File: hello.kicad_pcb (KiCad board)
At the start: 2 copper layers, 50 x 50 mm, 56 parts, among them J1 USB_OTG, J2 Conn_02x05_Odd_Even, J3 Conn_01x07, J4 Conn_01x04, Q1 DMG1012UW, Q2 DMG1012UW, Q3 DMG1012UW, Q4 DMG1012UW, Q5 DMG1012UW, Q6 NTR1P02T1G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

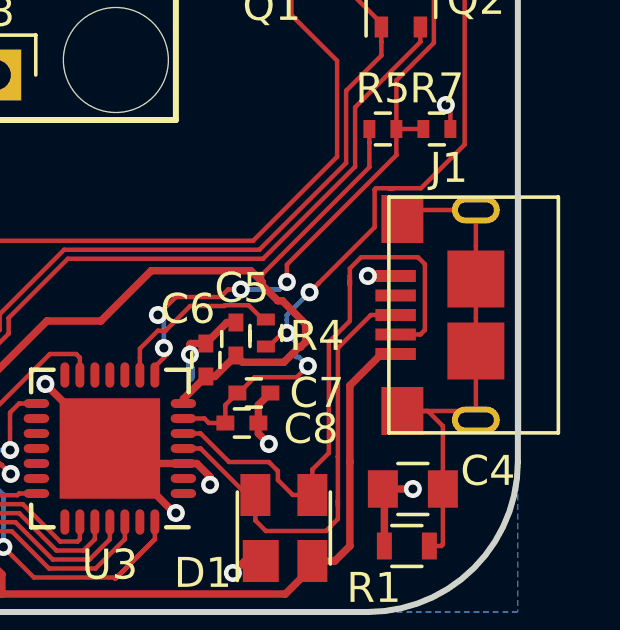
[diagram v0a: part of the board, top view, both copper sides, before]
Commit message: The mounting holes of the USB connector are 6.6mm apart, not 7mm.
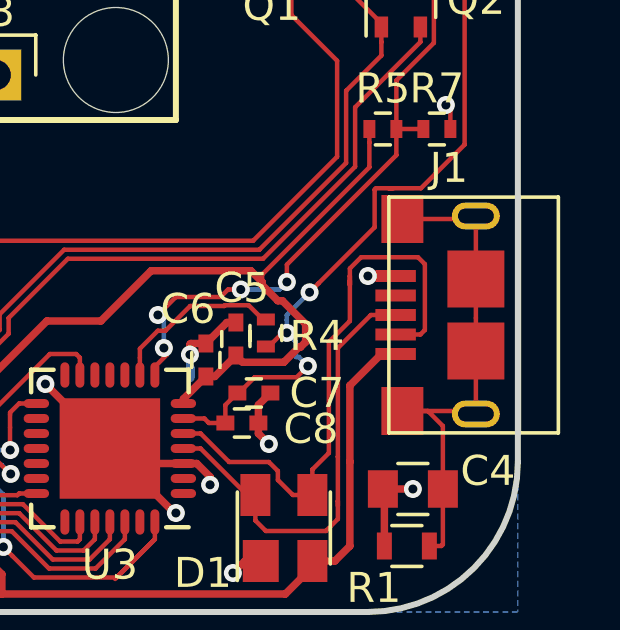
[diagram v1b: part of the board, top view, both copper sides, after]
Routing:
- net Net-(C4-Pad2): track 18.1 -> 17.6 mm
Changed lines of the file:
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@@
     (thickness 1.6)
     (drawings 24)
-    (tracks 1301)
+    (tracks 1300)
     (zones 0)
     (modules 56)
@@
     (add_net VBUS)
   )
+  (module hello:USB_Micro-B_10118193-0001LF (layer F.Cu)
+    (at 123.6 115.1 90)
+    (descr "Micro USB Type B Receptacle")
+    (tags "USB USB_B USB_micro USB_OTG")
+    (attr smd)
+    (fp_text reference J1 (at 4.9 -0.9 180) (layer F.SilkS)
+      (effects (font (size 1 1) (thickness 0.15)))
+    )
+    (fp_text value USB_OTG (at 0 5.01 90) (layer F.Fab)
+      (effects (font (size 1 1) (thickness 0.15)))
+    )
+    (fp_line (start -4.18 -3.6) (end 4.18 -3.6) (layer F.CrtYd) (width 0.05))
+    (fp_line (start 4.18 -3.6) (end 4.18 3) (layer F.CrtYd) (width 0.05))
+    (fp_line (start 4.18 3) (end -4.18 3) (layer F.CrtYd) (width 0.05))
+    (fp_line (start -4.18 3) (end -4.18 -3.6) (layer F.CrtYd) (width 0.05))
+    (fp_line (start -3.93 2.75) (end 3.93 2.75) (layer F.SilkS) (width 0.12))
+    (fp_line (start -3.93 -2.9) (end 3.93 -2.9) (layer F.SilkS) (width 0.12))
+    (fp_line (start 3.93 -2.9) (end 3.93 2.75) (layer F.SilkS) (width 0.12))
+    (fp_line (start 3.93 1.45) (end -3.93 1.45) (layer F.SilkS) (width 0.12))
+    (fp_line (start -3.93 2.75) (end -3.93 -2.9) (layer F.SilkS) (width 0.12))
+    (pad 1 smd rect (at -1.3 -2.675 180) (size 1.35 0.4) (layers F.Cu F.Paste F.Mask)
+      (net 5 VBUS))
+    (pad 2 smd rect (at -0.65 -2.675 180) (size 1.35 0.4) (layers F.Cu F.Paste F.Mask)
+      (net 84 /D-))
+    (pad 3 smd rect (at 0 -2.675 180) (size 1.35 0.4) (layers F.Cu F.Paste F.Mask)
+      (net 83 /D+))
+    (pad 4 smd rect (at 0.65 -2.675 180) (size 1.35 0.4) (layers F.Cu F.Paste F.Mask)
+      (net 10 "Net-(J1-Pad4)"))
+    (pad 5 smd rect (at 1.3 -2.675 180) (size 1.35 0.4) (layers F.Cu F.Paste F.Mask)
+      (net 2 GND))
+    (pad 6 smd rect (at -3.2 -2.45 90) (size 1.6 1.4) (layers F.Cu F.Paste F.Mask)
+      (net 4 "Net-(C4-Pad2)"))
+    (pad 6 smd rect (at 3.2 -2.45 90) (size 1.6 1.4) (layers F.Cu F.Paste F.Mask)
+      (net 4 "Net-(C4-Pad2)"))
+    (pad 6 thru_hole oval (at -3.3 0 180) (size 1.6 0.9) (drill oval 1.2 0.5) (layers *.Cu *.Mask)
+      (net 4 "Net-(C4-Pad2)"))
+    (pad 6 thru_hole oval (at 3.3 0 180) (size 1.6 0.9) (drill oval 1.2 0.5) (layers *.Cu *.Mask)
+      (net 4 "Net-(C4-Pad2)"))
+    (pad 6 smd rect (at -1.2 0 90) (size 1.9 1.9) (layers F.Cu F.Paste F.Mask)
+      (net 4 "Net-(C4-Pad2)"))
+    (pad 6 smd rect (at 1.2 0 90) (size 1.9 1.9) (layers F.Cu F.Paste F.Mask)
+      (net 4 "Net-(C4-Pad2)"))
+  )
   (module Housings_DFN_QFN:QFN-28-1EP_5x5mm_Pitch0.5mm (layer F.Cu)
     (at 111.4 119.55 180)
@@
       (rotate (xyz 0 0 0))
     )
-  )
-  (module hello:USB_Micro-B_10118193-0001LF (layer F.Cu)
-    (at 123.6 115.1 90)
-    (descr "Micro USB Type B Receptacle")
-    (tags "USB USB_B USB_micro USB_OTG")
-    (attr smd)
-    (fp_text reference J1 (at 4.9 -0.9 180) (layer F.SilkS)
-      (effects (font (size 1 1) (thickness 0.15)))
-    )
-    (fp_text value USB_OTG (at 0 5.01 90) (layer F.Fab)
-      (effects (font (size 1 1) (thickness 0.15)))
-    )
-    (fp_line (start -4.18 -3.6) (end 4.18 -3.6) (layer F.CrtYd) (width 0.05))
-    (fp_line (start 4.18 -3.6) (end 4.18 3) (layer F.CrtYd) (width 0.05))
-    (fp_line (start 4.18 3) (end -4.18 3) (layer F.CrtYd) (width 0.05))
-    (fp_line (start -4.18 3) (end -4.18 -3.6) (layer F.CrtYd) (width 0.05))
-    (fp_line (start -3.93 2.75) (end 3.93 2.75) (layer F.SilkS) (width 0.12))
-    (fp_line (start -3.93 -2.9) (end 3.93 -2.9) (layer F.SilkS) (width 0.12))
-    (fp_line (start 3.93 -2.9) (end 3.93 2.75) (layer F.SilkS) (width 0.12))
-    (fp_line (start 3.93 1.45) (end -3.93 1.45) (layer F.SilkS) (width 0.12))
-    (fp_line (start -3.93 2.75) (end -3.93 -2.9) (layer F.SilkS) (width 0.12))
-    (pad 1 smd rect (at -1.3 -2.675 180) (size 1.35 0.4) (layers F.Cu F.Paste F.Mask)
-      (net 5 VBUS))
-    (pad 2 smd rect (at -0.65 -2.675 180) (size 1.35 0.4) (layers F.Cu F.Paste F.Mask)
-      (net 84 /D-))
-    (pad 3 smd rect (at 0 -2.675 180) (size 1.35 0.4) (layers F.Cu F.Paste F.Mask)
-      (net 83 /D+))
-    (pad 4 smd rect (at 0.65 -2.675 180) (size 1.35 0.4) (layers F.Cu F.Paste F.Mask)
-      (net 10 "Net-(J1-Pad4)"))
-    (pad 5 smd rect (at 1.3 -2.675 180) (size 1.35 0.4) (layers F.Cu F.Paste F.Mask)
-      (net 2 GND))
-    (pad 6 smd rect (at -3.2 -2.45 90) (size 1.6 1.4) (layers F.Cu F.Paste F.Mask)
-      (net 4 "Net-(C4-Pad2)"))
-    (pad 6 smd rect (at 3.2 -2.45 90) (size 1.6 1.4) (layers F.Cu F.Paste F.Mask)
-      (net 4 "Net-(C4-Pad2)"))
-    (pad 6 thru_hole oval (at -3.5 0 180) (size 1.6 0.9) (drill oval 1.2 0.5) (layers *.Cu *.Mask)
-      (net 4 "Net-(C4-Pad2)"))
-    (pad 6 thru_hole oval (at 3.5 0 180) (size 1.6 0.9) (drill oval 1.2 0.5) (layers *.Cu *.Mask)
-      (net 4 "Net-(C4-Pad2)"))
-    (pad 6 smd rect (at -1.2 0 90) (size 1.9 1.9) (layers F.Cu F.Paste F.Mask)
-      (net 4 "Net-(C4-Pad2)"))
-    (pad 6 smd rect (at 1.2 0 90) (size 1.9 1.9) (layers F.Cu F.Paste F.Mask)
-      (net 4 "Net-(C4-Pad2)"))
   )
   (module Pin_Headers:Pin_Header_Straight_2x05_Pitch1.27mm (layer F.Cu)
@@
   (segment (start 80.05 90.1) (end 80.05 91.15) (width 0.25) (layer F.Cu) (net 3))
   (segment (start 80.05 91.15) (end 80.1 91.2) (width 0.25) (layer F.Cu) (net 3))
+  (segment (start 123.6 118.4) (end 123.6 116.3) (width 0.15) (layer F.Cu) (net 4))
+  (segment (start 121.15 118.3) (end 123.5 118.3) (width 0.15) (layer F.Cu) (net 4))
+  (segment (start 123.5 118.3) (end 123.6 118.4) (width 0.15) (layer F.Cu) (net 4))
+  (segment (start 123.6 111.8) (end 123.6 113.9) (width 0.15) (layer F.Cu) (net 4))
+  (segment (start 121.15 111.9) (end 123.5 111.9) (width 0.15) (layer F.Cu) (net 4))
+  (segment (start 123.5 111.9) (end 123.6 111.8) (width 0.15) (layer F.Cu) (net 4))
   (segment (start 122.5 120.9) (end 122.5 122.75) (width 0.15) (layer F.Cu) (net 4))
   (segment (start 122.5 122.75) (end 122.45 122.8) (width 0.15) (layer F.Cu) (net 4))
@@
   (segment (start 122.5 118.8) (end 122 118.3) (width 0.15) (layer F.Cu) (net 4))
   (segment (start 122 118.3) (end 121.15 118.3) (width 0.15) (layer F.Cu) (net 4))
-  (segment (start 123.6 111.6) (end 121.45 111.6) (width 0.15) (layer F.Cu) (net 4))
-  (segment (start 121.45 111.6) (end 121.15 111.9) (width 0.15) (layer F.Cu) (net 4))
-  (segment (start 123.6 113.9) (end 123.6 112.8) (width 0.15) (layer F.Cu) (net 4))
-  (segment (start 123.6 112.8) (end 123.6 111.6) (width 0.15) (layer F.Cu) (net 4))
   (segment (start 123.6 116.3) (end 123.6 115.2) (width 0.15) (layer F.Cu) (net 4))
   (segment (start 123.6 115.2) (end 123.6 113.9) (width 0.15) (layer F.Cu) (net 4))
-  (segment (start 123.6 118.6) (end 123.6 116.3) (width 0.15) (layer F.Cu) (net 4))
-  (segment (start 121.15 118.3) (end 123.3 118.3) (width 0.15) (layer F.Cu) (net 4))
-  (segment (start 123.3 118.3) (end 123.6 118.6) (width 0.15) (layer F.Cu) (net 4))
   (segment (start 107.4 117.2) (end 109.3 115.3) (width 0.25) (layer F.Cu) (net 5))
   (segment (start 109.3 115.3) (end 111.1 115.3) (width 0.25) (layer F.Cu) (net 5))

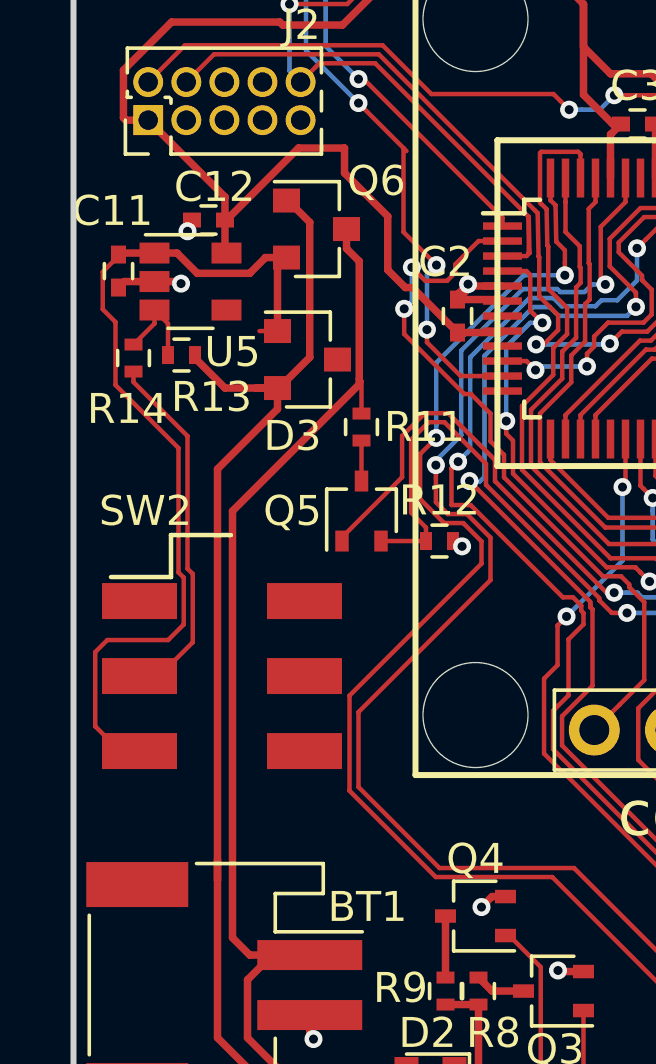
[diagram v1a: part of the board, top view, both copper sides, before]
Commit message: Fix pinout for BAS116 diode (D3)
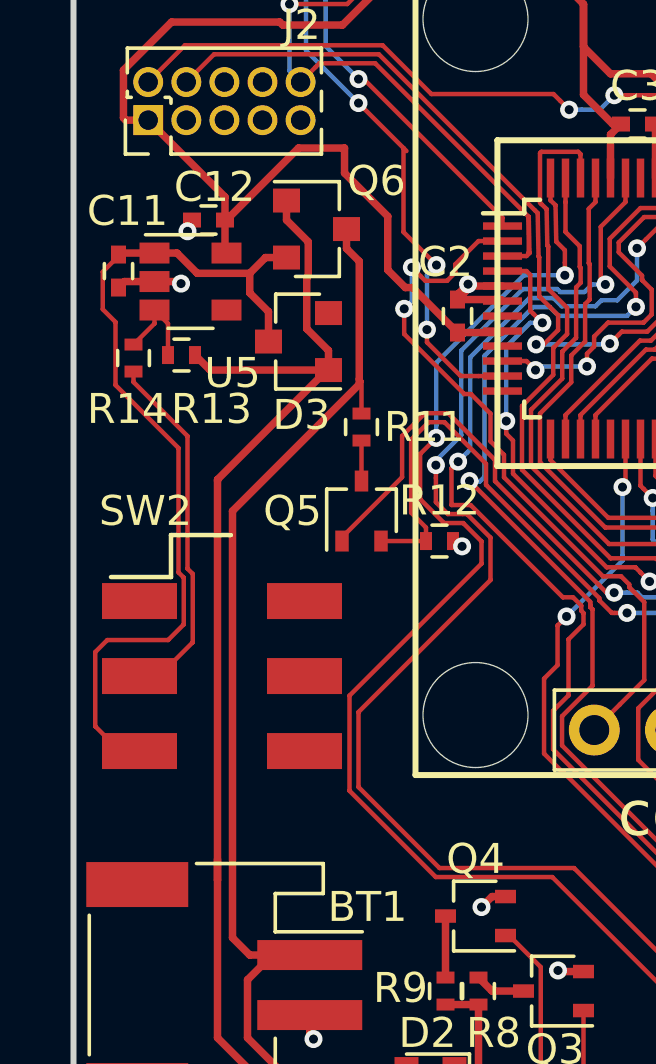
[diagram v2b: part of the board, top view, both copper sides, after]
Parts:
- moved D3 0.67 mm to (82.5, 94.2), turned to 180 degrees
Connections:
- D3 pad 1: Net-(C11-Pad1) -> VBUS
- D3 pad 2: VBUS -> (no net)
- D3 pad 3: (no net) -> Net-(C11-Pad1)
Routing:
- net VBUS: track 124.8 -> 126.1 mm
- net Net-(C11-Pad1): track 30.6 -> 30.0 mm
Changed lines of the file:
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@@
     (links 142)
     (no_connects 0)
-    (area 64.997618 72.175 131.321429 138.521428)
+    (area 74.899999 74.899999 125.100001 125.100001)
     (thickness 1.6)
     (drawings 24)
-    (tracks 1300)
+    (tracks 1303)
     (zones 0)
     (modules 56)
@@
   )
   (setup
-    (last_trace_width 0.15)
+    (last_trace_width 0.25)
     (user_trace_width 0.15)
     (user_trace_width 0.25)
@@
     (tags "capacitor 0402")
     (attr smd)
-    (fp_text reference C11 (at -2 0.2 360) (layer F.SilkS)
+    (fp_text reference C11 (at -2 -0.3 360) (layer F.SilkS)
       (effects (font (size 1 1) (thickness 0.15)))
     )
@@
       (effects (font (size 1 1) (thickness 0.15)))
     )
-    (fp_text user %R (at -2 0.2 360) (layer F.Fab)
+    (fp_text user %R (at -2 -0.3 360) (layer F.Fab)
       (effects (font (size 1 1) (thickness 0.15)))
     )
@@
   )
   (module TO_SOT_Packages_SMD:SOT-23 (layer F.Cu)
-    (at 82.8 94.75)
+    (at 82.5 94.15 180)
     (descr "SOT-23, Standard")
     (tags SOT-23)
     (attr smd)
-    (fp_text reference D3 (at -0.5 2.55) (layer F.SilkS)
-      (effects (font (size 1 1) (thickness 0.15)))
-    )
-    (fp_text value BAS116 (at 2.8 0.95) (layer F.Fab)
-      (effects (font (size 1 1) (thickness 0.15)))
-    )
-    (fp_text user %R (at 0 0 90) (layer F.Fab)
+    (fp_text reference D3 (at -0.1 -2.45 180) (layer F.SilkS)
+      (effects (font (size 1 1) (thickness 0.15)))
+    )
+    (fp_text value BAS116 (at -2 -1.15 180) (layer F.Fab)
+      (effects (font (size 1 1) (thickness 0.15)))
+    )
+    (fp_text user %R (at 0 0 270) (layer F.Fab)
       (effects (font (size 0.5 0.5) (thickness 0.075)))
     )
@@
     (fp_line (start 0.76 -1.58) (end -1.4 -1.58) (layer F.SilkS) (width 0.12))
     (fp_line (start 0.76 1.58) (end -0.7 1.58) (layer F.SilkS) (width 0.12))
-    (pad 1 smd rect (at -1 -0.95) (size 0.9 0.8) (layers F.Cu F.Paste F.Mask)
+    (pad 1 smd rect (at -1 -0.95 180) (size 0.9 0.8) (layers F.Cu F.Paste F.Mask)
+      (net 5 VBUS))
+    (pad 2 smd rect (at -1 0.95 180) (size 0.9 0.8) (layers F.Cu F.Paste F.Mask))
+    (pad 3 smd rect (at 1 0 180) (size 0.9 0.8) (layers F.Cu F.Paste F.Mask)
       (net 7 "Net-(C11-Pad1)"))
-    (pad 2 smd rect (at -1 0.95) (size 0.9 0.8) (layers F.Cu F.Paste F.Mask)
-      (net 5 VBUS))
-    (pad 3 smd rect (at 1 0) (size 0.9 0.8) (layers F.Cu F.Paste F.Mask))
     (model ${KISYS3DMOD}/TO_SOT_Packages_SMD.3dshapes/SOT-23.wrl
       (at (xyz 0 0 0))
@@
     (tags "resistor 0402")
     (attr smd)
-    (fp_text reference R13 (at -1 -1.4 180) (layer F.SilkS)
+    (fp_text reference R13 (at -1 -1.8 180) (layer F.SilkS)
       (effects (font (size 1 1) (thickness 0.15)))
     )
@@
       (effects (font (size 1 1) (thickness 0.15)))
     )
-    (fp_text user %R (at -1 -1.4 180) (layer F.Fab)
+    (fp_text user %R (at -1 -1.8 180) (layer F.Fab)
       (effects (font (size 1 1) (thickness 0.15)))
     )
@@
     (tags TSOP-5)
     (attr smd)
-    (fp_text reference U5 (at 1.4 2.35) (layer F.SilkS)
+    (fp_text reference U5 (at 1.4 3.05) (layer F.SilkS)
       (effects (font (size 1 1) (thickness 0.15)))
     )
@@
   (segment (start 123.6 116.3) (end 123.6 115.2) (width 0.15) (layer F.Cu) (net 4))
   (segment (start 123.6 115.2) (end 123.6 113.9) (width 0.15) (layer F.Cu) (net 4))
+  (segment (start 83.5 95.1) (end 79.55 95.1) (width 0.25) (layer F.Cu) (net 5))
+  (segment (start 79.55 95.1) (end 79.05 94.6) (width 0.25) (layer F.Cu) (net 5))
+  (segment (start 83.5 95.1) (end 83.5 94.45) (width 0.25) (layer F.Cu) (net 5))
+  (segment (start 83.5 94.45) (end 82.774999 93.724999) (width 0.25) (layer F.Cu) (net 5))
+  (segment (start 82.774999 93.724999) (end 82.774999 92.020003) (width 0.25) (layer F.Cu) (net 5))
+  (segment (start 82.774999 92.020003) (end 82.825001 91.970001) (width 0.25) (layer F.Cu) (net 5))
+  (segment (start 82.825001 91.970001) (end 82.825001 90.825001) (width 0.25) (layer F.Cu) (net 5))
+  (segment (start 82.1 90.1) (end 82.1 89.45) (width 0.25) (layer F.Cu) (net 5))
+  (segment (start 82.825001 90.825001) (end 82.1 90.1) (width 0.25) (layer F.Cu) (net 5))
+  (segment (start 79.8 112.1) (end 79.8 98.8) (width 0.25) (layer F.Cu) (net 5))
+  (segment (start 83.5 95.1) (end 83.45 95.1) (width 0.25) (layer F.Cu) (net 5))
+  (segment (start 83.45 95.1) (end 79.8 98.75) (width 0.25) (layer F.Cu) (net 5))
+  (segment (start 79.8 98.75) (end 79.8 98.8) (width 0.25) (layer F.Cu) (net 5))
   (segment (start 107.4 117.2) (end 109.3 115.3) (width 0.25) (layer F.Cu) (net 5))
   (segment (start 109.3 115.3) (end 111.1 115.3) (width 0.25) (layer F.Cu) (net 5))
@@
   (segment (start 120.45 116.4) (end 119.400022 117.449978) (width 0.25) (layer F.Cu) (net 5))
   (segment (start 120.925 116.4) (end 120.45 116.4) (width 0.25) (layer F.Cu) (net 5))
-  (segment (start 79.8 112.1) (end 79.8 98.4) (width 0.25) (layer F.Cu) (net 5))
-  (segment (start 79.8 98.4) (end 81.8 96.4) (width 0.25) (layer F.Cu) (net 5))
-  (segment (start 81.8 96.4) (end 81.8 95.7) (width 0.25) (layer F.Cu) (net 5))
-  (segment (start 81.8 95.7) (end 81.75 95.7) (width 0.25) (layer F.Cu) (net 5))
   (segment (start 84.389999 122.575001) (end 85.925001 122.575001) (width 0.25) (layer F.Cu) (net 5))
   (segment (start 84.324999 122.510001) (end 84.389999 122.575001) (width 0.25) (layer F.Cu) (net 5))
@@
   (segment (start 79.8 112.1) (end 79.8 117.358912) (width 0.25) (layer F.Cu) (net 5))
   (segment (start 79.8 111.4) (end 79.8 112.1) (width 0.25) (layer F.Cu) (net 5))
-  (segment (start 81.8 95.7) (end 80.05 95.7) (width 0.25) (layer F.Cu) (net 5))
-  (segment (start 80.05 95.7) (end 79.05 94.7) (width 0.25) (layer F.Cu) (net 5))
   (segment (start 79.05 94.7) (end 79.05 94.6) (width 0.25) (layer F.Cu) (net 5))
-  (segment (start 81.8 95.7) (end 81.85 95.7) (width 0.25) (layer F.Cu) (net 5))
-  (segment (start 82.875001 90.175001) (end 82.15 89.45) (width 0.25) (layer F.Cu) (net 5))
-  (segment (start 81.85 95.7) (end 82.875001 94.674999) (width 0.25) (layer F.Cu) (net 5))
-  (segment (start 82.875001 94.674999) (end 82.875001 90.175001) (width 0.25) (layer F.Cu) (net 5))
   (segment (start 82.15 89.45) (end 82.1 89.45) (width 0.25) (layer F.Cu) (net 5))
-  (segment (start 81.8 95.7) (end 81.1 95.7) (width 0.25) (layer F.Cu) (net 5))
   (segment (start 86.55 123.3) (end 86.55 123.4) (width 0.25) (layer F.Cu) (net 5))
   (segment (start 86.55 123.4) (end 86.925001 123.775001) (width 0.25) (layer F.Cu) (net 5))
@@
   (segment (start 120.269999 110.874999) (end 120.224999 110.919999) (width 0.15) (layer F.Cu) (net 6))
   (via (at 118.056594 114.343406) (size 0.6) (drill 0.3) (layers F.Cu B.Cu) (net 6))
+  (segment (start 81.5 94.15) (end 81.5 93.154998) (width 0.25) (layer F.Cu) (net 7))
+  (segment (start 81.5 93.154998) (end 80.874999 92.529997) (width 0.25) (layer F.Cu) (net 7))
+  (segment (start 80.874999 92.529997) (end 80.874999 91.875001) (width 0.25) (layer F.Cu) (net 7))
+  (segment (start 82.05 91.35) (end 82.1 91.35) (width 0.15) (layer F.Cu) (net 7))
   (segment (start 75.724999 104.5) (end 75.724999 106.974999) (width 0.15) (layer F.Cu) (net 7))
   (segment (start 78.155002 104.1) (end 76.124999 104.1) (width 0.15) (layer F.Cu) (net 7))
@@
   (segment (start 75.724999 106.974999) (end 76.55 107.8) (width 0.15) (layer F.Cu) (net 7))
   (segment (start 76.55 107.8) (end 77.2 107.8) (width 0.15) (layer F.Cu) (net 7))
-  (segment (start 81.8 93.8) (end 81.2 93.8) (width 0.15) (layer F.Cu) (net 7))
   (segment (start 77.7 91.2) (end 78.45 91.2) (width 0.25) (layer F.Cu) (net 7))
   (segment (start 78.45 91.2) (end 79.125001 91.875001) (width 0.25) (layer F.Cu) (net 7))
@@
   (segment (start 80.874999 91.875001) (end 81.4 91.35) (width 0.25) (layer F.Cu) (net 7))
   (segment (start 81.4 91.35) (end 82.1 91.35) (width 0.25) (layer F.Cu) (net 7))
-  (segment (start 81.8 93.8) (end 81.8 91.65) (width 0.25) (layer F.Cu) (net 7))
-  (segment (start 81.8 91.65) (end 82.1 91.35) (width 0.25) (layer F.Cu) (net 7))
   (segment (start 77.7 91.2) (end 76.55 91.2) (width 0.25) (layer F.Cu) (net 7))
   (segment (start 76.55 91.2) (end 76.5 91.25) (width 0.25) (layer F.Cu) (net 7))

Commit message: Update version number to 1b
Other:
- board text added: "hello version 1b coolfactor.org"
- board text removed: "hello version 1 coolfactor.org"
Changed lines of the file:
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@@
   )
   (setup
-    (last_trace_width 0.25)
+    (last_trace_width 0.15)
     (user_trace_width 0.15)
     (user_trace_width 0.25)
@@
   (gr_line (start 113.6 85.5) (end 113.6 104.5) (layer B.SilkS) (width 0.2))
   (gr_line (start 86.4 85.5) (end 113.6 85.5) (layer B.SilkS) (width 0.2))
-  (gr_text "hello\nversion 1\ncoolfactor.org" (at 111.7 115.5) (layer B.SilkS)
+  (gr_text "hello\nversion 1b\ncoolfactor.org" (at 111.7 115.5) (layer B.SilkS)
     (effects (font (size 1.5 1.5) (thickness 0.3)) (justify left mirror))
   )
